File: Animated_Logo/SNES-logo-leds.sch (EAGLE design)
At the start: 9 parts

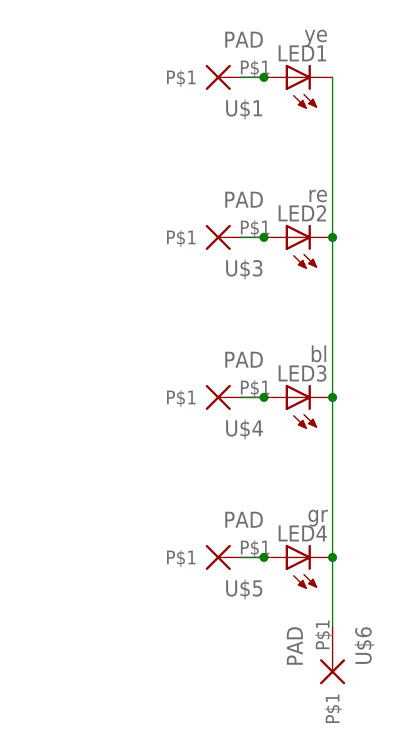
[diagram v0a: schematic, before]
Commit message: Minor updates for the Logo-PCBs: - move resistors for LEDs to the LED PCB - LEDs can be either in 0805 or P-LCC-2 package
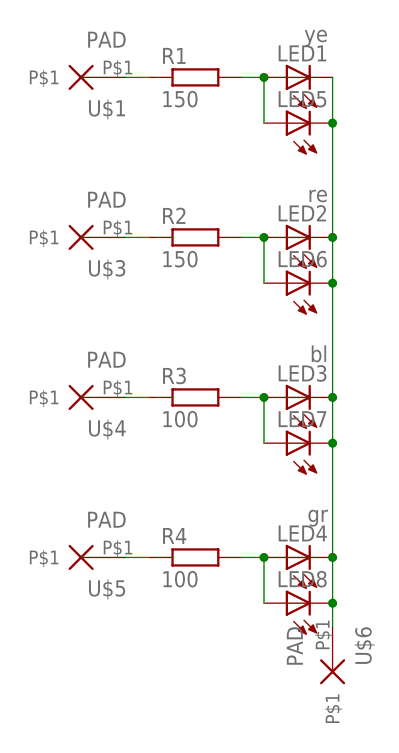
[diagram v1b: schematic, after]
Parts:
- added LED5, LED6, LED7, LED8: (no value), led:LEDP-LCC-2
- added R1, R2: 150, snes_div:R0805
- added R3, R4: 100, snes_div:R0805
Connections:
- new net N$2: R2.1, U$3.P$1
- new net N$4: R1.1, U$1.P$1
- new net N$5: R3.1, U$4.P$1
- new net N$6: R4.1, U$5.P$1
- net N$1: now also LED5.C, LED6.C, LED7.C, LED8.C
- net N$20: now also LED6.A, R2.2; no longer U$3.P$1
- net N$21: now also LED7.A, R3.2; no longer U$4.P$1
- net N$22: now also LED8.A, R4.2; no longer U$5.P$1
- net N$3: now also LED5.A, R1.2; no longer U$1.P$1
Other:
- moved on the sheet: U$1, U$3, U$4, U$5
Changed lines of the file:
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@@
 <?xml version="1.0" encoding="utf-8"?>
 <!DOCTYPE eagle SYSTEM "eagle.dtd">
-<eagle version="7.2.0">
+<eagle version="7.3.0">
 <drawing>
 <settings>
@@
 <part name="U$5" library="MS_Mod" deviceset="PAD" device=""/>
 <part name="U$6" library="MS_Mod" deviceset="PAD" device=""/>
+<part name="R2" library="snes_div" deviceset="R0805" device="" value="150"/>
+<part name="R1" library="snes_div" deviceset="R0805" device="" value="150"/>
+<part name="R3" library="snes_div" deviceset="R0805" device="" value="100"/>
+<part name="R4" library="snes_div" deviceset="R0805" device="" value="100"/>
+<part name="LED5" library="led" deviceset="LED" device="P-LCC-2"/>
+<part name="LED6" library="led" deviceset="LED" device="P-LCC-2"/>
+<part name="LED7" library="led" deviceset="LED" device="P-LCC-2"/>
+<part name="LED8" library="led" deviceset="LED" device="P-LCC-2"/>
 </parts>
 <sheets>
@@
 <instance part="LED3" gate="G$1" x="12.7" y="33.02" rot="R90"/>
 <instance part="LED4" gate="G$1" x="12.7" y="15.24" rot="R90"/>
-<instance part="U$1" gate="G$1" x="5.08" y="68.58" rot="R180"/>
-<instance part="U$3" gate="G$1" x="5.08" y="50.8" rot="R180"/>
-<instance part="U$4" gate="G$1" x="5.08" y="33.02" rot="R180"/>
-<instance part="U$5" gate="G$1" x="5.08" y="15.24" rot="R180"/>
+<instance part="U$1" gate="G$1" x="-10.16" y="68.58" rot="R180"/>
+<instance part="U$3" gate="G$1" x="-10.16" y="50.8" rot="R180"/>
+<instance part="U$4" gate="G$1" x="-10.16" y="33.02" rot="R180"/>
+<instance part="U$5" gate="G$1" x="-10.16" y="15.24" rot="R180"/>
 <instance part="U$6" gate="G$1" x="17.78" y="2.54" rot="R270"/>
+<instance part="R2" gate="G$1" x="2.54" y="50.8"/>
+<instance part="R1" gate="G$1" x="2.54" y="68.58"/>
+<instance part="R3" gate="G$1" x="2.54" y="33.02"/>
+<instance part="R4" gate="G$1" x="2.54" y="15.24"/>
+<instance part="LED5" gate="G$1" x="12.7" y="63.5" rot="R90"/>
+<instance part="LED6" gate="G$1" x="12.7" y="45.72" rot="R90"/>
+<instance part="LED7" gate="G$1" x="12.7" y="27.94" rot="R90"/>
+<instance part="LED8" gate="G$1" x="12.7" y="10.16" rot="R90"/>
 </instances>
 <busses>
@@
 <net name="N$1" class="0">
 <segment>
-<wire x1="17.78" y1="7.62" x2="17.78" y2="15.24" width="0.1524" layer="91"/>
-<wire x1="17.78" y1="15.24" x2="17.78" y2="33.02" width="0.1524" layer="91"/>
-<wire x1="17.78" y1="33.02" x2="17.78" y2="50.8" width="0.1524" layer="91"/>
-<wire x1="17.78" y1="50.8" x2="17.78" y2="68.58" width="0.1524" layer="91"/>
+<wire x1="17.78" y1="7.62" x2="17.78" y2="10.16" width="0.1524" layer="91"/>
+<wire x1="17.78" y1="10.16" x2="17.78" y2="15.24" width="0.1524" layer="91"/>
+<wire x1="17.78" y1="15.24" x2="17.78" y2="27.94" width="0.1524" layer="91"/>
+<wire x1="17.78" y1="27.94" x2="17.78" y2="33.02" width="0.1524" layer="91"/>
+<wire x1="17.78" y1="33.02" x2="17.78" y2="45.72" width="0.1524" layer="91"/>
+<wire x1="17.78" y1="45.72" x2="17.78" y2="50.8" width="0.1524" layer="91"/>
+<wire x1="17.78" y1="50.8" x2="17.78" y2="63.5" width="0.1524" layer="91"/>
 <junction x="17.78" y="50.8"/>
 <junction x="17.78" y="33.02"/>
@@
 <pinref part="LED4" gate="G$1" pin="C"/>
 <pinref part="U$6" gate="G$1" pin="P$1"/>
+<pinref part="LED5" gate="G$1" pin="C"/>
+<wire x1="17.78" y1="63.5" x2="17.78" y2="68.58" width="0.1524" layer="91"/>
+<junction x="17.78" y="63.5"/>
+<pinref part="LED6" gate="G$1" pin="C"/>
+<junction x="17.78" y="45.72"/>
+<pinref part="LED7" gate="G$1" pin="C"/>
+<junction x="17.78" y="27.94"/>
+<pinref part="LED8" gate="G$1" pin="C"/>
+<junction x="17.78" y="10.16"/>
 </segment>
 </net>
@@
 <pinref part="LED1" gate="G$1" pin="A"/>
 <pinref part="LED1" gate="G$1" pin="A"/>
-<wire x1="7.62" y1="68.58" x2="10.16" y2="68.58" width="0.1524" layer="91"/>
+<pinref part="R1" gate="G$1" pin="2"/>
+<wire x1="10.16" y1="68.58" x2="7.62" y2="68.58" width="0.1524" layer="91"/>
 <junction x="10.16" y="68.58"/>
-<pinref part="U$1" gate="G$1" pin="P$1"/>
+<pinref part="LED5" gate="G$1" pin="A"/>
+<wire x1="10.16" y1="63.5" x2="10.16" y2="68.58" width="0.1524" layer="91"/>
 </segment>
 </net>
@@
 <pinref part="LED2" gate="G$1" pin="A"/>
 <pinref part="LED2" gate="G$1" pin="A"/>
+<pinref part="R2" gate="G$1" pin="2"/>
 <wire x1="7.62" y1="50.8" x2="10.16" y2="50.8" width="0.1524" layer="91"/>
 <junction x="10.16" y="50.8"/>
-<pinref part="U$3" gate="G$1" pin="P$1"/>
+<pinref part="LED6" gate="G$1" pin="A"/>
+<wire x1="10.16" y1="45.72" x2="10.16" y2="50.8" width="0.1524" layer="91"/>
 </segment>
 </net>
@@
 <pinref part="LED3" gate="G$1" pin="A"/>
 <pinref part="LED3" gate="G$1" pin="A"/>
+<junction x="10.16" y="33.02"/>
+<pinref part="R3" gate="G$1" pin="2"/>
 <wire x1="7.62" y1="33.02" x2="10.16" y2="33.02" width="0.1524" layer="91"/>
-<junction x="10.16" y="33.02"/>
-<pinref part="U$4" gate="G$1" pin="P$1"/>
+<pinref part="LED7" gate="G$1" pin="A"/>
+<wire x1="10.16" y1="27.94" x2="10.16" y2="33.02" width="0.1524" layer="91"/>
 </segment>
 </net>
@@
 <pinref part="LED4" gate="G$1" pin="A"/>
 <pinref part="LED4" gate="G$1" pin="A"/>
+<junction x="10.16" y="15.24"/>
+<pinref part="R4" gate="G$1" pin="2"/>
 <wire x1="7.62" y1="15.24" x2="10.16" y2="15.24" width="0.1524" layer="91"/>
-<junction x="10.16" y="15.24"/>
+<pinref part="LED8" gate="G$1" pin="A"/>
+<wire x1="10.16" y1="10.16" x2="10.16" y2="15.24" width="0.1524" layer="91"/>
+</segment>
+</net>
+<net name="N$2" class="0">
+<segment>
+<pinref part="R2" gate="G$1" pin="1"/>
+<pinref part="U$3" gate="G$1" pin="P$1"/>
+<wire x1="-2.54" y1="50.8" x2="-5.08" y2="50.8" width="0.1524" layer="91"/>
+</segment>
+</net>
+<net name="N$4" class="0">
+<segment>
+<pinref part="R1" gate="G$1" pin="1"/>
+<pinref part="U$1" gate="G$1" pin="P$1"/>
+<wire x1="-2.54" y1="68.58" x2="-5.08" y2="68.58" width="0.1524" layer="91"/>
+</segment>
+</net>
+<net name="N$5" class="0">
+<segment>
+<pinref part="R3" gate="G$1" pin="1"/>
+<pinref part="U$4" gate="G$1" pin="P$1"/>
+<wire x1="-5.08" y1="33.02" x2="-2.54" y2="33.02" width="0.1524" layer="91"/>
+</segment>
+</net>
+<net name="N$6" class="0">
+<segment>
+<pinref part="R4" gate="G$1" pin="1"/>
 <pinref part="U$5" gate="G$1" pin="P$1"/>
-</segment>
-</net>
+<wire x1="-5.08" y1="15.24" x2="-2.54" y2="15.24" width="0.1524" layer="91"/>
+</segment>
+</net>
